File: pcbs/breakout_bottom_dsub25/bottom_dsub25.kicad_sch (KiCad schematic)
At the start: 26 parts, among them J1 DB25_Pins, J2 Conn_01x12, J3 Conn_01x12, J4 Screw_Terminal_01x06, J5 Screw_Terminal_01x06, J7 Conn_01x04, J8 Conn_01x04, J8_Z1 Conn_01x06_Pin, J8_Z2 Conn_01x06_Pin, J8_Z3 Conn_01x06_Pin

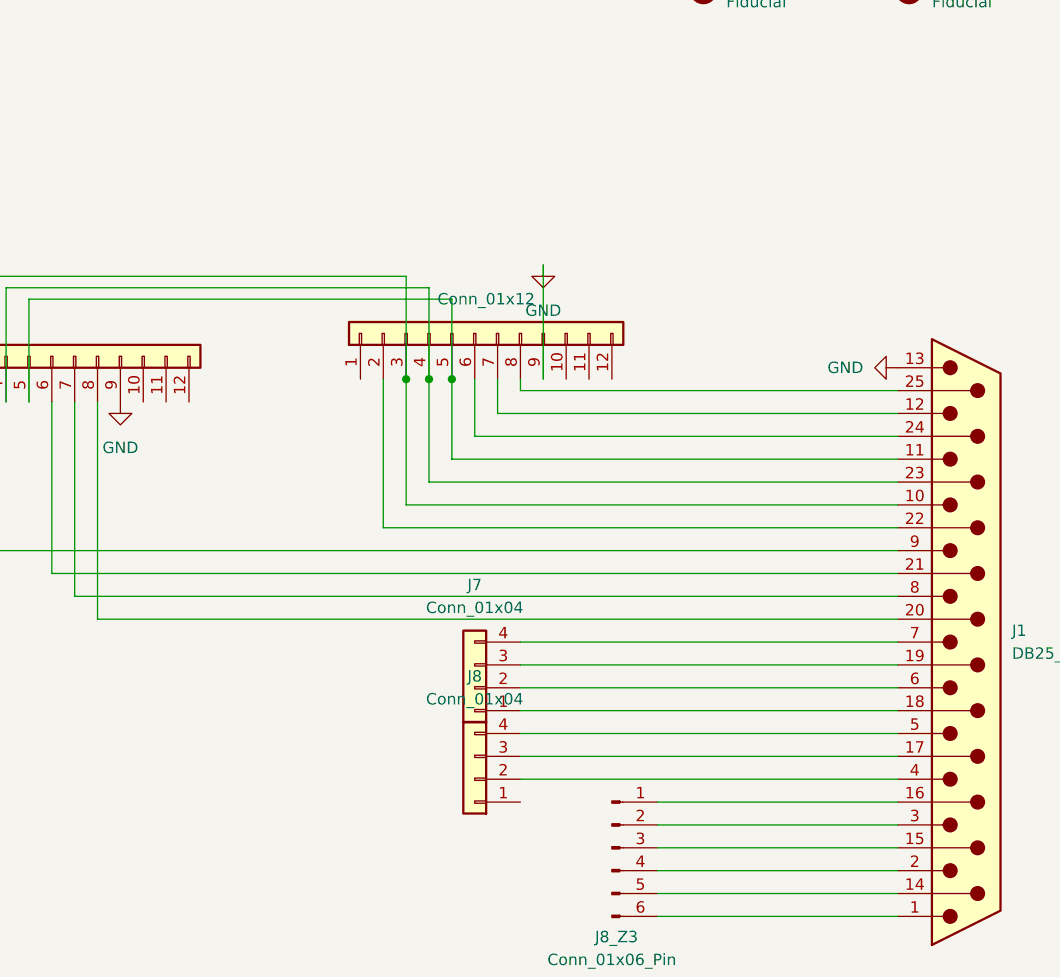
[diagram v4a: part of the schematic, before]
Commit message: wire-in the 24V from the main board + wire ground on this pin
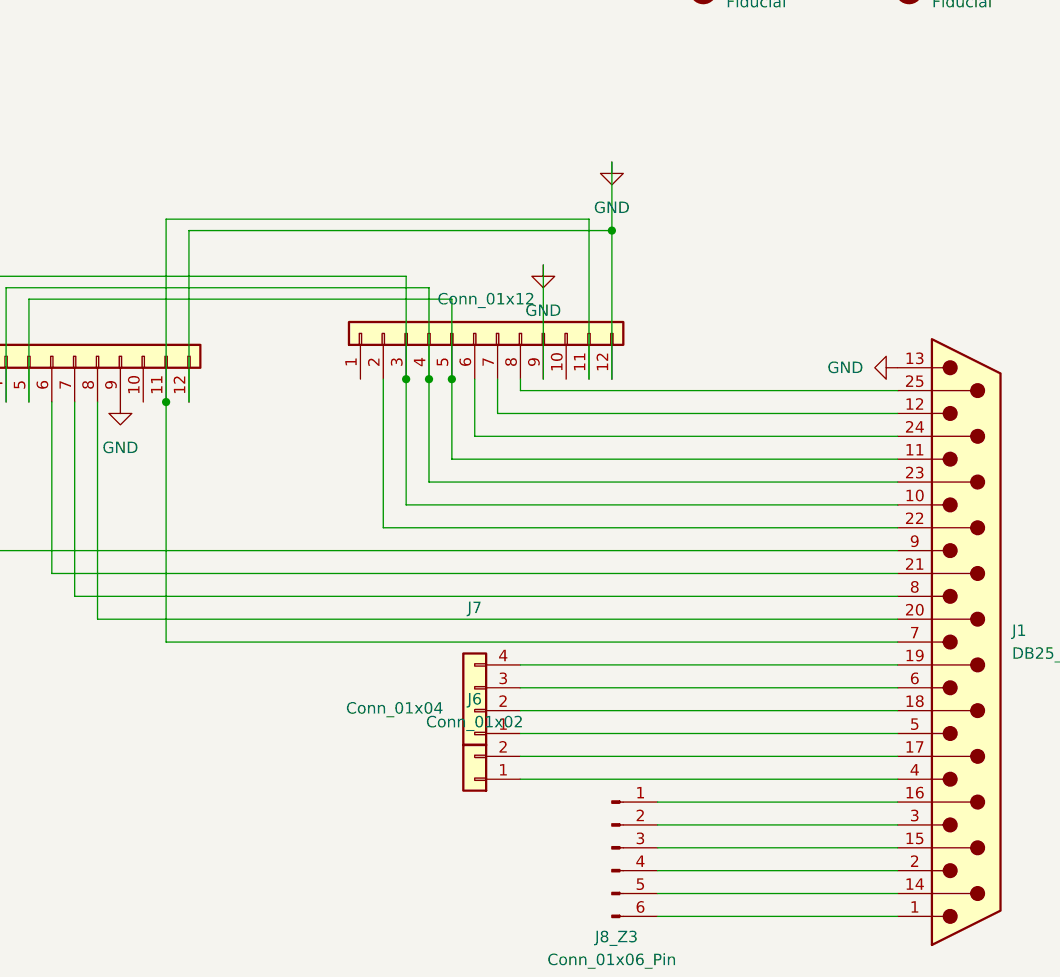
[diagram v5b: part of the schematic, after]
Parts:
- removed J8: Conn_01x04, Connector_JST:JST_XH_B4B-XH-A_1x04_P2.50mm_Vertical, symbol Connector_Generic:Conn_01x04
- added J6: Conn_01x02, Connector_JST:JST_XH_B2B-XH-A_1x02_P2.50mm_Vertical, symbol Connector_Generic:Conn_01x02
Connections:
- net GND: now also J2.12 (Pin_12), J3.12 (Pin_12)
- net at J1.17 (P17): now also J6.2 (Pin_2)
- net at J1.18 (P18): now also J7.2 (Pin_2); no longer J7.1 (Pin_1)
- net at J1.19 (P19): now also J7.4 (Pin_4); no longer J7.3 (Pin_3)
- net at J1.4: now also J6.1 (Pin_1)
- net at J1.5: now also J7.1 (Pin_1)
- net at J1.6: now also J7.3 (Pin_3); no longer J7.2 (Pin_2)
- net at J1.7: now also J2.11 (Pin_11), J3.11 (Pin_11); no longer J7.4 (Pin_4)
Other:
- moved on the sheet: J7
